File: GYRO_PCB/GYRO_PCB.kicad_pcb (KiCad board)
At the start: 2 copper layers, 70.5 x 83 mm, 18 parts, among them J1 Pmod GYRO, J2 FLASH Socket 1, J3 FLASH Socket 2, J4 Power Terminal, J5 Battery Switch, U1 NUCLEO64-F446RE

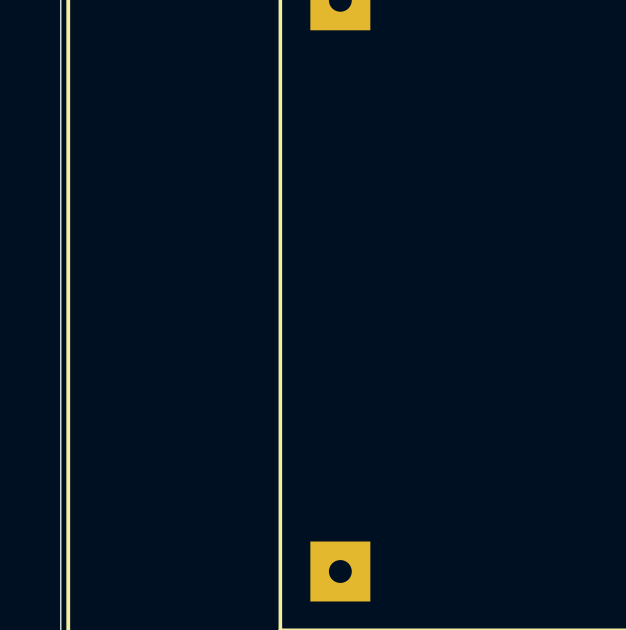
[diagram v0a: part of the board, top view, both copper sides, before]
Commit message: feat: add push button
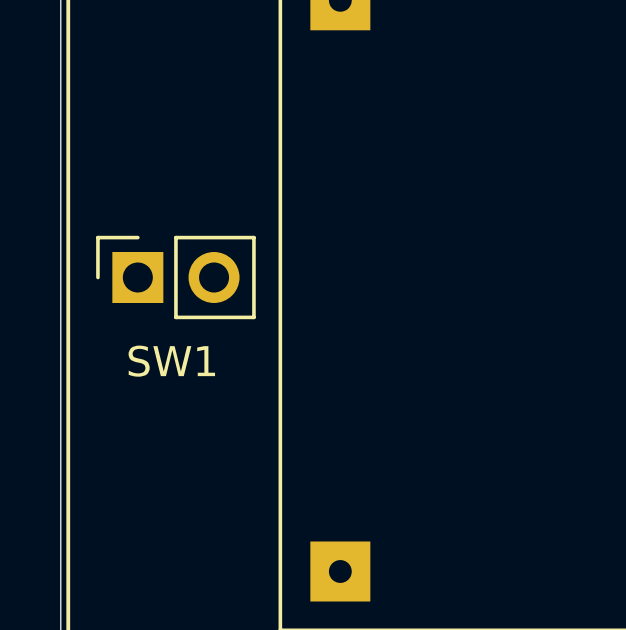
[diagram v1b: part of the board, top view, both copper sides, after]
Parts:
- added SW1: SW_Push, Connector_PinSocket_2.54mm:PinSocket_1x02_P2.54mm_Vertical, F.Cu at (114.0, 63.4)
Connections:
- U1 pad CN7_1: unconnected-(U1-PC10-PadCN7_1) -> PUSH_BUTTON
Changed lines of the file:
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@@
 	(net 60 "unconnected-(U1-U5V-PadCN10_8)")
 	(net 61 "unconnected-(U1-PD2-PadCN7_4)")
-	(net 62 "unconnected-(U1-PC10-PadCN7_1)")
+	(net 62 "PUSH_BUTTON")
 	(net 63 "unconnected-(U1-PC6-PadCN10_4)")
 	(net 64 "unconnected-(U1-PB6-PadCN10_17)")
@@
 			(layers "*.Cu" "*.Mask")
 			(remove_unused_layers no)
-			(net 62 "unconnected-(U1-PC10-PadCN7_1)")
+			(net 62 "PUSH_BUTTON")
 			(pinfunction "PC10")
-			(pintype "bidirectional+no_connect")
+			(pintype "bidirectional")
 			(solder_mask_margin 0.102)
 		)
@@
 			)
 		)
+	)
+	(footprint "Connector_PinSocket_2.54mm:PinSocket_1x02_P2.54mm_Vertical"
+		(layer "F.Cu")
+		(at 113.95 63.395 90)
+		(descr "Through hole straight socket strip, 1x02, 2.54mm pitch, single row (from Kicad 4.0.7), script generated")
+		(tags "Through hole socket strip THT 1x02 2.54mm single row")
+		(property "Reference" "SW1"
+			(at -2.825 1.15 0)
+			(layer "F.SilkS")
+			(effects
+				(font
+					(size 1 1)
+					(thickness 0.15)
+				)
+			)
+		)
+		(property "Value" "SW_Push"
+			(at 0 5.31 90)
+			(layer "F.Fab")
+			(hide yes)
+			(effects
+				(font
+					(size 1 1)
+					(thickness 0.15)
+				)
+			)
+		)
+		(property "Datasheet" "~"
+			(at 0 0 90)
+			(layer "F.Fab")
+			(hide yes)
+			(effects
+				(font
+					(size 1.27 1.27)
+					(thickness 0.15)
+				)
+			)
+		)
+		(property "Description" "Push button switch, generic, two pins"
+			(at 0 0 90)
+			(layer "F.Fab")
+			(hide yes)
+			(effects
+				(font
+					(size 1.27 1.27)
+					(thickness 0.15)
+				)
+			)
+		)
+		(sheetname "/")
+		(sheetfile "GYRO_PCB.kicad_sch")
+		(attr through_hole)
+		(fp_line
+			(start 1.33 -1.33)
+			(end 1.33 0)
+			(stroke
+				(width 0.12)
+				(type solid)
+			)
+			(layer "F.SilkS")
+		)
+		(fp_line
+			(start 0 -1.33)
+			(end 1.33 -1.33)
+			(stroke
+				(width 0.12)
+				(type solid)
+			)
+			(layer "F.SilkS")
+		)
+		(fp_line
+			(start 1.33 1.27)
+			(end 1.33 3.87)
+			(stroke
+				(width 0.12)
+				(type solid)
+			)
+			(layer "F.SilkS")
+		)
+		(fp_line
+			(start -1.33 1.27)
+			(end 1.33 1.27)
+			(stroke
+				(width 0.12)
+				(type solid)
+			)
+			(layer "F.SilkS")
+		)
+		(fp_line
+			(start -1.33 1.27)
+			(end -1.33 3.87)
+			(stroke
+				(width 0.12)
+				(type solid)
+			)
+			(layer "F.SilkS")
+		)
+		(fp_line
+			(start -1.33 3.87)
+			(end 1.33 3.87)
+			(stroke
+				(width 0.12)
+				(type solid)
+			)
+			(layer "F.SilkS")
+		)
+		(fp_line
+			(start 1.75 -1.8)
+			(end 1.75 4.3)
+			(stroke
+				(width 0.05)
+				(type solid)
+			)
+			(layer "F.CrtYd")
+		)
+		(fp_line
+			(start -1.8 -1.8)
+			(end 1.75 -1.8)
+			(stroke
+				(width 0.05)
+				(type solid)
+			)
+			(layer "F.CrtYd")
+		)
+		(fp_line
+			(start 1.75 4.3)
+			(end -1.8 4.3)
+			(stroke
+				(width 0.05)
+				(type solid)
+			)
+			(layer "F.CrtYd")
+		)
+		(fp_line
+			(start -1.8 4.3)
+			(end -1.8 -1.8)
+			(stroke
+				(width 0.05)
+				(type solid)
+			)
+			(layer "F.CrtYd")
+		)
+		(fp_line
+			(start 0.635 -1.27)
+			(end 1.27 -0.635)
+			(stroke
+				(width 0.1)
+				(type solid)
+			)
+			(layer "F.Fab")
+		)
+		(fp_line
+			(start -1.27 -1.27)
+			(end 0.635 -1.27)
+			(stroke
+				(width 0.1)
+				(type solid)
+			)
+			(layer "F.Fab")
+		)
+		(fp_line
+			(start 1.27 -0.635)
+			(end 1.27 3.81)
+			(stroke
+				(width 0.1)
+				(type solid)
+			)
+			(layer "F.Fab")
+		)
+		(fp_line
+			(start 1.27 3.81)
+			(end -1.27 3.81)
+			(stroke
+				(width 0.1)
+				(type solid)
+			)
+			(layer "F.Fab")
+		)
+		(fp_line
+			(start -1.27 3.81)
+			(end -1.27 -1.27)
+			(stroke
+				(width 0.1)
+				(type solid)
+			)
+			(layer "F.Fab")
+		)
+		(pad "1" thru_hole rect
+			(at 0 0 90)
+			(size 1.7 1.7)
+			(drill 1)
+			(layers "*.Cu" "*.Mask")
+			(remove_unused_layers no)
+			(net 62 "PUSH_BUTTON")
+			(pinfunction "1")
+			(pintype "passive")
+		)
+		(pad "2" thru_hole circle
+			(at 0 2.54 90)
+			(size 1.7 1.7)
+			(drill 1)
+			(layers "*.Cu" "*.Mask")
+			(remove_unused_layers no)
+			(net 18 "GND")
+			(pinfunction "2")
+			(pintype "passive")
+		)
+		(embedded_fonts no)
+		(model "${KICAD9_3DMODEL_DIR}/Connector_PinSocket_2.54mm.3dshapes/PinSocket_1x02_P2.54mm_Vertical.step"
+			(offset
+				(xyz 0 0 0)
+			)
+			(scale
+				(xyz 1 1 1)
+			)
+			(rotate
+				(xyz 0 0 0)
+			)
+		)

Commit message: feat: routing done
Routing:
- net NUCLEO_FLASH_SPI2_MISO: track 0.00 -> 50.8 mm
- net NUCLEO_GYRO_I2C1_SDA: track 0.00 -> 29.0 mm
- net NUCLEO_FLASH_SPI2_MOSI: track 0.00 -> 26.6 mm
- net NUCLEO_GYRO_I2C1_SCL: track 0.00 -> 25.3 mm
- net NUCLEO_FLASH_CS: track 0.00 -> 23.4 mm
- net NUCLEO_FLASH_SCLK: track 0.00 -> 22.5 mm
- net PUSH_BUTTON: track 0.00 -> 18.3 mm
- net NUCLEO_E5V: track 0.00 -> 15.2 mm
- net LED: track 0.00 -> 15.0 mm
- net Net-(D1-A): track 0.00 -> 9.12 mm
- net Net-(J4-Pin_1): track 0.00 -> 8.72 mm
- net BAT: track 0.00 -> 8.56 mm
- net Net-(J3-W#/DQ2): track 0.00 -> 6.35 mm
- net Net-(J2-RESET#): track 0.00 -> 5.74 mm
- net Net-(J2-DQ3/HOLD#): track 0.00 -> 5.61 mm
- added copper zone on F.Cu, net +3V3
- added copper zone on B.Cu, net GND

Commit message: feat: add footprints
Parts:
- added G***: LOGO, FOOTPRINTS:mexico, F.Cu at (142.9, 63.7)
- added G***: LOGO, FOOTPRINTS:diego_logo, B.Cu at (146.5, 66.3)

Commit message: fix: change logo
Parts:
- moved G*** 1.81 mm to (144.6, 66.3)
